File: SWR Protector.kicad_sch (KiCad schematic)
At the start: 28 parts, among them J1 Barrel_Jack, J2 Barrel_Jack, J3 Conn_02x03, J3 transceiver, J4 antenna, K2 ATX209, Q1 2N3904, T1 1:12, T2 1:12, U1 LM78L05_TO92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

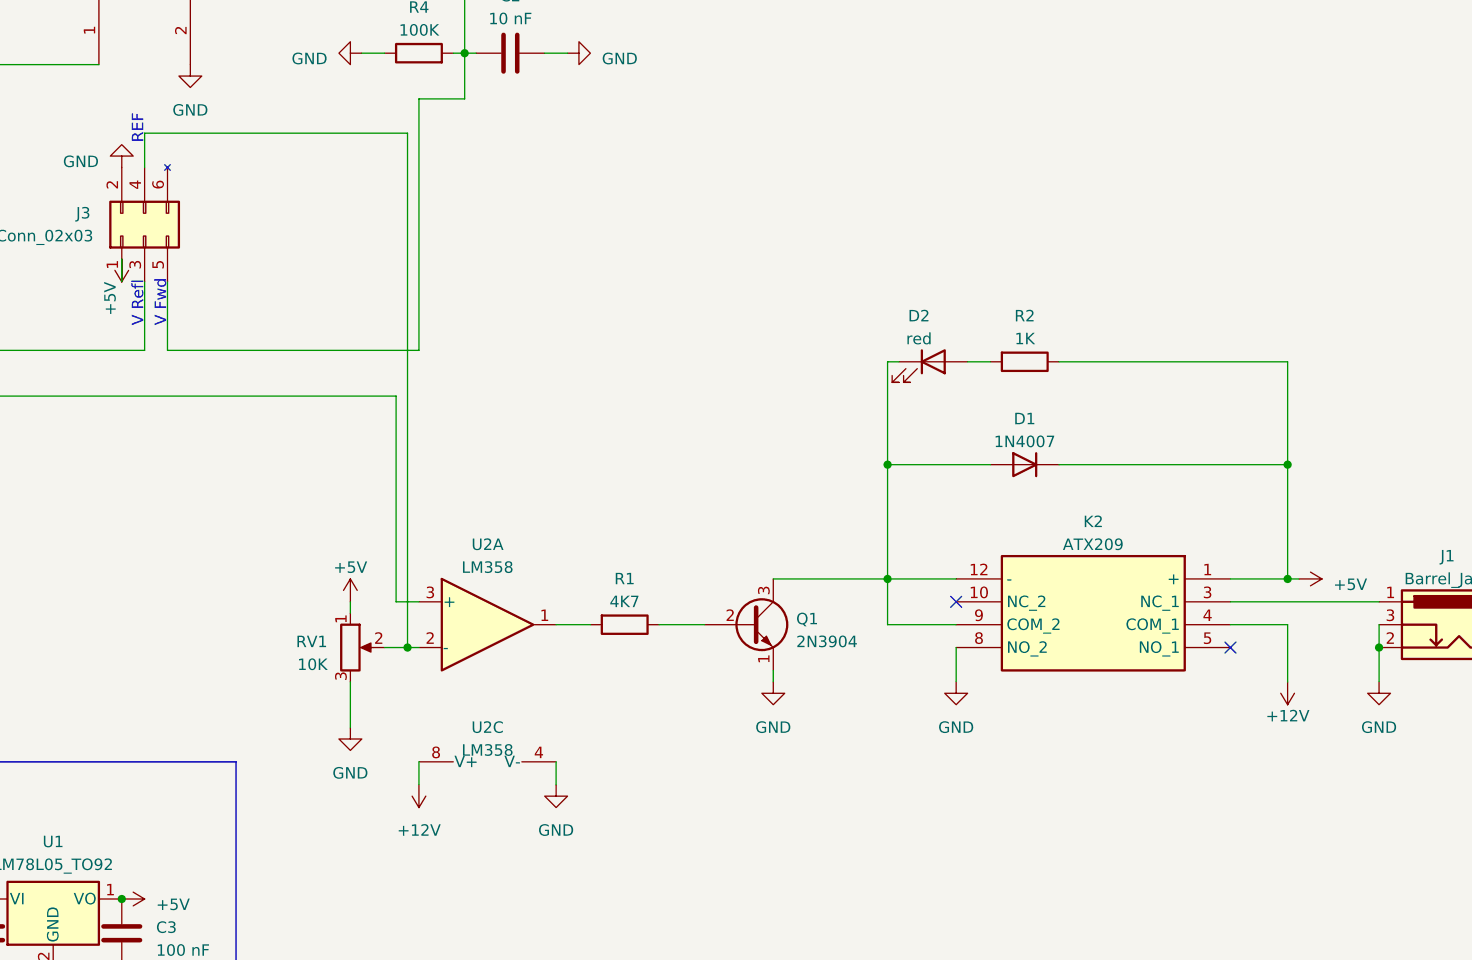
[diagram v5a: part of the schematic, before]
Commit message: The George Option complete. George asked for a buzzer when relay trips.  Used 12V part w/ same footprint. That thing is HUGE.  I can see already I want a jumper to disable it after I build one to test.
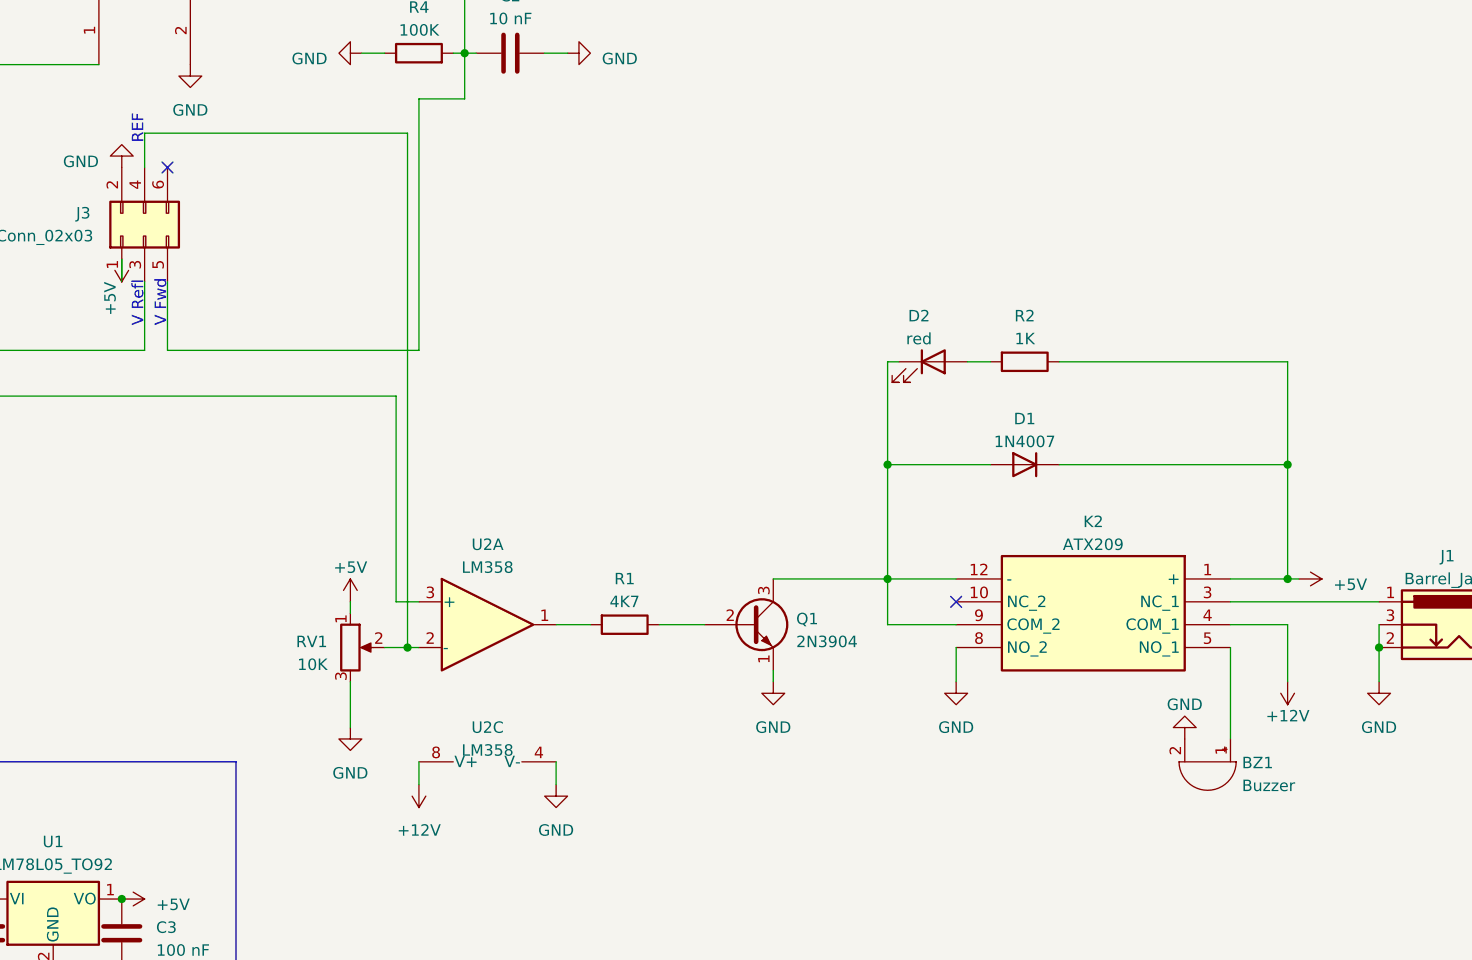
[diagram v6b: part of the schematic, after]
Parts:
- added BZ1: Buzzer, Buzzer_Beeper:Buzzer_12x9.5RM7.6, symbol Device:Buzzer
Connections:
- net GND: now also BZ1.2 (+)
- net at K2.5 (NO_1): now also BZ1.1 (-)
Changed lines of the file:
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@@
     (title "SWR Protector WA7GIL")
     (date "2023-05-28")
-    (rev "v1.3")
+    (rev "v1.4")
   )
   (junction (at 44.45 179.07) (diameter 0) (color 0 0 0 0)
@@
   (junction (at 50.8 60.96) (diameter 0) (color 0 0 0 0)
   )
+  (no_connect (at 101.6 92.71))
   (no_connect (at 189.23 140.97))
-  (no_connect (at 219.71 146.05))
   (wire (pts (xy 242.57 34.29) (xy 242.57 39.37))
     (stroke (width 0) (type default))
@@
   )
   (wire (pts (xy 134.62 80.01) (xy 134.62 85.09))
+    (stroke (width 0) (type default))
+  )
+  (wire (pts (xy 219.71 146.05) (xy 219.71 156.21))
     (stroke (width 0) (type default))
   )
@@
         (path "/5ddb5305-6e1d-4af3-a40a-20431dc1473c"
           (reference "C1") (unit 1)
+        )
+      )
+    )
+  )
+  (symbol (lib_id "Device:Buzzer") (at 217.17 158.75 270) (unit 1)
+    (in_bom yes) (on_board yes) (dnp no) (fields_autoplaced)
+    (property "Reference" "BZ1" (at 220.98 158.8701 90)
+      (effects (font (size 1.27 1.27)) (justify left))
+    )
+    (property "Value" "Buzzer" (at 220.98 161.4101 90)
+      (effects (font (size 1.27 1.27)) (justify left))
+    )
+    (property "Footprint" "Buzzer_Beeper:Buzzer_12x9.5RM7.6" (at 219.71 158.115 90)
+      (effects (font (size 1.27 1.27)) hide)
+    )
+    (property "Datasheet" "~" (at 219.71 158.115 90)
+      (effects (font (size 1.27 1.27)) hide)
+    )
+    (pin "1")
+    (pin "2")
+    (instances
+      (project "SWR Protector"
+        (path "/5ddb5305-6e1d-4af3-a40a-20431dc1473c"
+          (reference "BZ1") (unit 1)
         )
       )
@@
         )
       )
+    )
+  )
+  (symbol (lib_id "power:GND") (at 214.63 156.21 180) (unit 1)
+    (in_bom yes) (on_board yes) (dnp no) (fields_autoplaced)
+    (property "Reference" "#PWR031" (at 214.63 149.86 0)
+      (effects (font (size 1.27 1.27)) hide)
+    )
+    (property "Value" "GND" (at 214.63 152.4 0)
+      (effects (font (size 1.27 1.27)))
+    )
+    (property "Footprint" "" (at 214.63 156.21 0)
+      (effects (font (size 1.27 1.27)) hide)
+    )
+    (property "Datasheet" "" (at 214.63 156.21 0)
+      (effects (font (size 1.27 1.27)) hide)
+    )
+    (pin "1")
+    (instances
+      (project "SWR Protector"
+        (path "/5ddb5305-6e1d-4af3-a40a-20431dc1473c"
+          (reference "#PWR031") (unit 1)
+        )
+      )

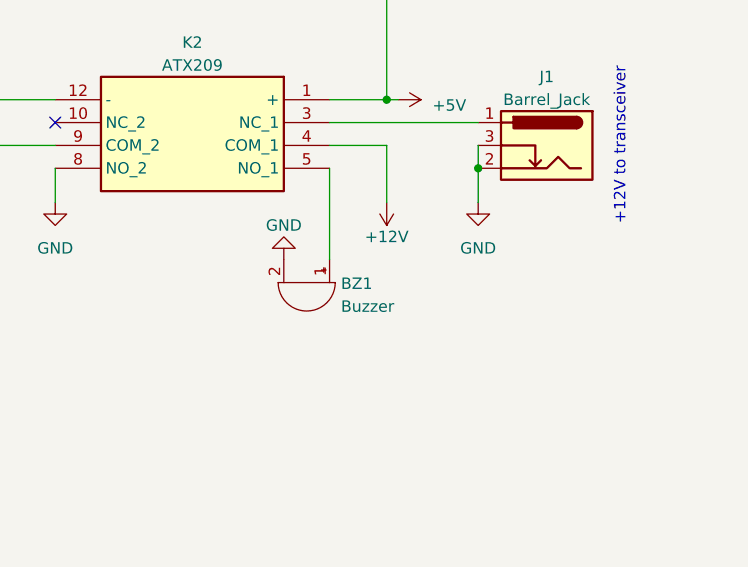
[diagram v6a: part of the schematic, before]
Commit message: add jumper to disable George buzzer
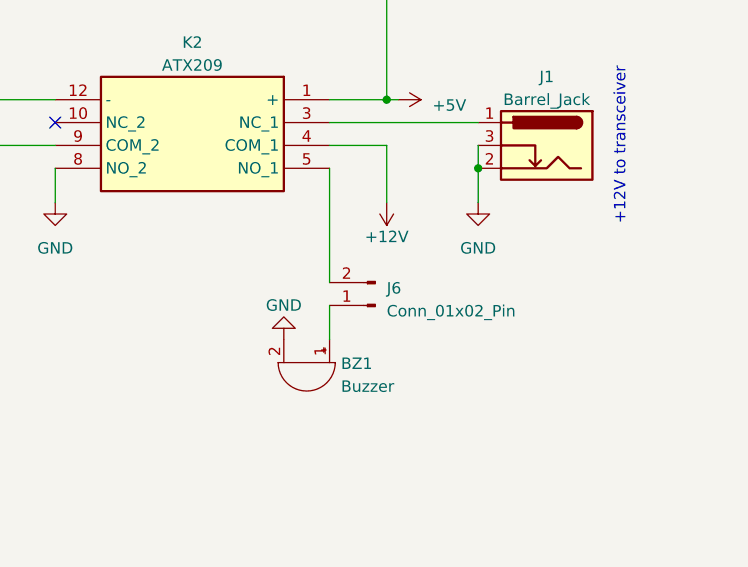
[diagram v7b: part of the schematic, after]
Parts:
- added J6: Conn_01x02_Pin, Connector_PinHeader_2.54mm:PinHeader_1x02_P2.54mm_Vertical, symbol Connector:Conn_01x02_Pin
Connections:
- net at BZ1.1 (-): now also J6.1 (Pin_1); no longer K2.5 (NO_1)
- new net: J6.2 (Pin_2), K2.5 (NO_1)
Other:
- moved on the sheet: BZ1
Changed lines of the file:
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@@
     (title "SWR Protector WA7GIL")
     (date "2023-05-28")
-    (rev "v1.4")
+    (rev "v1.5")
   )
   (junction (at 44.45 179.07) (diameter 0) (color 0 0 0 0)
@@
     (stroke (width 0) (type default))
   )
+  (wire (pts (xy 219.71 161.29) (xy 219.71 165.1))
+    (stroke (width 0) (type default))
+  )
   (wire (pts (xy 182.88 114.3) (xy 181.61 114.3))
     (stroke (width 0) (type default))
@@
     (stroke (width 0) (type default))
   )
-  (wire (pts (xy 219.71 146.05) (xy 219.71 156.21))
+  (wire (pts (xy 219.71 146.05) (xy 219.71 158.75))
     (stroke (width 0) (type default))
   )
@@
     )
   )
+  (symbol (lib_id "Connector:Conn_01x02_Pin") (at 224.79 161.29 180) (unit 1)
+    (in_bom yes) (on_board yes) (dnp no) (fields_autoplaced)
+    (property "Reference" "J6" (at 226.06 159.385 0)
+      (effects (font (size 1.27 1.27)) (justify right))
+    )
+    (property "Value" "Conn_01x02_Pin" (at 226.06 161.925 0)
+      (effects (font (size 1.27 1.27)) (justify right))
+    )
+    (property "Footprint" "Connector_PinHeader_2.54mm:PinHeader_1x02_P2.54mm_Vertical" (at 224.79 161.29 0)
+      (effects (font (size 1.27 1.27)) hide)
+    )
+    (property "Datasheet" "~" (at 224.79 161.29 0)
+      (effects (font (size 1.27 1.27)) hide)
+    )
+    (pin "1")
+    (pin "2")
+    (instances
+      (project "SWR Protector"
+        (path "/5ddb5305-6e1d-4af3-a40a-20431dc1473c"
+          (reference "J6") (unit 1)
+        )
+      )
+    )
+  )
   (symbol (lib_id "power:GND") (at 121.92 154.94 0) (unit 1)
     (in_bom yes) (on_board yes) (dnp no) (fields_autoplaced)
@@
     )
   )
-  (symbol (lib_id "Device:Buzzer") (at 217.17 158.75 270) (unit 1)
-    (in_bom yes) (on_board yes) (dnp no) (fields_autoplaced)
-    (property "Reference" "BZ1" (at 220.98 158.8701 90)
+  (symbol (lib_id "Device:Buzzer") (at 217.17 167.64 270) (unit 1)
+    (in_bom yes) (on_board yes) (dnp no) (fields_autoplaced)
+    (property "Reference" "BZ1" (at 220.98 167.7601 90)
       (effects (font (size 1.27 1.27)) (justify left))
     )
-    (property "Value" "Buzzer" (at 220.98 161.4101 90)
+    (property "Value" "Buzzer" (at 220.98 170.3001 90)
       (effects (font (size 1.27 1.27)) (justify left))
     )
-    (property "Footprint" "Buzzer_Beeper:Buzzer_12x9.5RM7.6" (at 219.71 158.115 90)
-      (effects (font (size 1.27 1.27)) hide)
-    )
-    (property "Datasheet" "~" (at 219.71 158.115 90)
+    (property "Footprint" "Buzzer_Beeper:Buzzer_12x9.5RM7.6" (at 219.71 167.005 90)
+      (effects (font (size 1.27 1.27)) hide)
+    )
+    (property "Datasheet" "~" (at 219.71 167.005 90)
       (effects (font (size 1.27 1.27)) hide)
     )
@@
     )
   )
-  (symbol (lib_id "power:GND") (at 214.63 156.21 180) (unit 1)
-    (in_bom yes) (on_board yes) (dnp no) (fields_autoplaced)
-    (property "Reference" "#PWR031" (at 214.63 149.86 0)
-      (effects (font (size 1.27 1.27)) hide)
-    )
-    (property "Value" "GND" (at 214.63 152.4 0)
-      (effects (font (size 1.27 1.27)))
-    )
-    (property "Footprint" "" (at 214.63 156.21 0)
-      (effects (font (size 1.27 1.27)) hide)
-    )
-    (property "Datasheet" "" (at 214.63 156.21 0)
-      (effects (font (size 1.27 1.27)) hide)
-    )
+  (symbol (lib_id "power:GND") (at 214.63 165.1 180) (unit 1)
+    (in_bom yes) (on_board yes) (dnp no) (fields_autoplaced)
+    (property "Reference" "#PWR031" (at 214.63 158.75 0)
+      (effects (font (size 1.27 1.27)) hide)
+    )
+    (property "Value" "GND" (at 214.63 161.29 0)
+      (effects (font (size 1.27 1.27)))
+    )
+    (property "Footprint" "" (at 214.63 165.1 0)
+      (effects (font (size 1.27 1.27)) hide)
+    )
+    (property "Datasheet" "" (at 214.63 165.1 0)
+      (effects (font (size 1.27 1.27)) hide)
+    )

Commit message: Change 10K trimpot from Bourne to PT10.  Different pinout, vastly cheaper. Started picking up a warning about copper slivers.  Found one that was an acute wedge, so I widened the trace to slop over it.  Others still elude me.
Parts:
- RV1: footprint Potentiometer_THT:Potentiometer_Bourns_3266Y_Vertical -> Potentiometer_THT:Potentiometer_Piher_PT-10-V05_Vertical
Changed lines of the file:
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@@
     (title "SWR Protector WA7GIL")
     (date "2023-05-28")
-    (rev "v1.5")
+    (rev "v1.6")
   )
   (junction (at 44.45 179.07) (diameter 0) (color 0 0 0 0)
@@
       (effects (font (size 1.27 1.27)) (justify right))
     )
-    (property "Footprint" "Potentiometer_THT:Potentiometer_Bourns_3266Y_Vertical" (at 121.92 146.05 0)
-      (effects (font (size 1.27 1.27)) hide)
-    )
+    (property "Footprint" "Potentiometer_THT:Potentiometer_Piher_PT-10-V05_Vertical" (at 121.92 146.05 0)
+      (effects (font (size 1.27 1.27)) hide)
+    )
